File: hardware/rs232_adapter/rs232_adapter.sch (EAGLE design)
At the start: 9 parts, among them IC1 MAX202ECWE

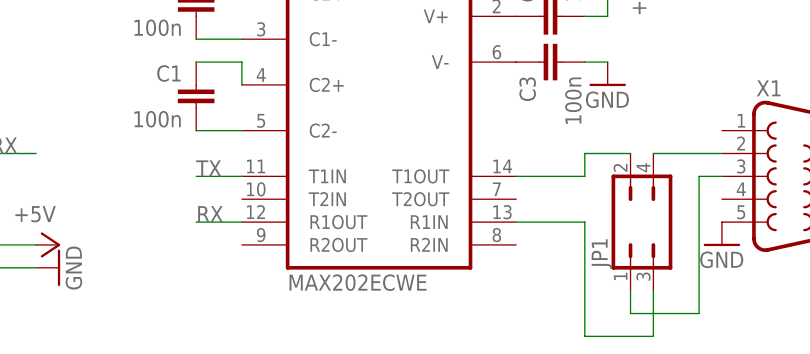
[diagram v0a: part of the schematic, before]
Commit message: change the package of the max202 and add some documentation
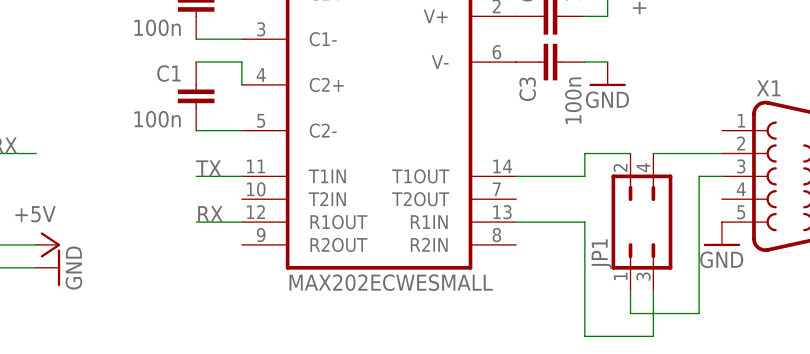
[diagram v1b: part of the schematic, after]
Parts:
- IC1: value MAX202ECWE -> MAX202ECWESMALL; device maxim:MAX202ECWE -> maxim:MAX202ECWESMALL
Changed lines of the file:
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@@
 <part name="GND3" library="supply1" deviceset="GND" device=""/>
 <part name="GND4" library="supply1" deviceset="GND" device=""/>
-<part name="IC1" library="maxim" deviceset="MAX202ECWE" device=""/>
 <part name="C1" library="rcl" deviceset="C-EU" device="C0805" value="100n"/>
 <part name="C2" library="rcl" deviceset="C-EU" device="C0805" value="100n"/>
@@
 <part name="X1" library="con-subd" deviceset="F09" device="HP"/>
 <part name="GND6" library="supply1" deviceset="GND" device=""/>
+<part name="IC1" library="maxim" deviceset="MAX202ECWE" device="SMALL"/>
 </parts>
 <sheets>
@@
 <instance part="GND3" gate="1" x="0" y="7.62" rot="R270"/>
 <instance part="GND4" gate="1" x="30.48" y="7.62" rot="R90"/>
-<instance part="IC1" gate="G$1" x="66.04" y="25.4"/>
 <instance part="C1" gate="G$1" x="45.72" y="27.94" rot="MR0"/>
 <instance part="C2" gate="G$1" x="45.72" y="38.1" rot="MR0"/>
-<instance part="IC1" gate="P" x="63.5" y="55.88"/>
 <instance part="C3" gate="G$1" x="83.82" y="30.48" rot="MR270"/>
 <instance part="GND1" gate="1" x="91.44" y="27.94"/>
@@
 <instance part="X1" gate="G$1" x="111.76" y="17.78"/>
 <instance part="GND6" gate="1" x="104.14" y="10.16"/>
+<instance part="IC1" gate="G$1" x="66.04" y="25.4"/>
+<instance part="IC1" gate="P" x="63.5" y="55.88"/>
 </instances>
 <busses>
@@
 </segment>
 <segment>
-<pinref part="IC1" gate="G$1" pin="R1OUT"/>
 <wire x1="50.8" y1="12.7" x2="45.72" y2="12.7" width="0.1524" layer="91"/>
 <label x="45.72" y="12.7" size="1.778" layer="95"/>
+<pinref part="IC1" gate="G$1" pin="R1OUT"/>
 </segment>
 </net>
@@
 </segment>
 <segment>
-<pinref part="IC1" gate="G$1" pin="T1IN"/>
 <wire x1="50.8" y1="17.78" x2="45.72" y2="17.78" width="0.1524" layer="91"/>
 <label x="45.72" y="17.78" size="1.778" layer="95"/>
+<pinref part="IC1" gate="G$1" pin="T1IN"/>
 </segment>
 </net>
@@
 <pinref part="SV2" gate="G$1" pin="17"/>
 <wire x1="2.54" y1="10.16" x2="7.62" y2="10.16" width="0.1524" layer="91"/>
-</segment>
-<segment>
-<pinref part="IC1" gate="P" pin="VCC"/>
-<pinref part="P+1" gate="1" pin="+5V"/>
 </segment>
 <segment>
@@
 <pinref part="P+3" gate="1" pin="+5V"/>
 </segment>
+<segment>
+<pinref part="P+1" gate="1" pin="+5V"/>
+<pinref part="IC1" gate="P" pin="VCC"/>
+</segment>
 </net>
 <net name="GND" class="0">
@@
 </segment>
 <segment>
-<pinref part="IC1" gate="P" pin="GND"/>
-<pinref part="GND2" gate="1" pin="GND"/>
-</segment>
-<segment>
 <pinref part="C5" gate="G$1" pin="2"/>
 <pinref part="GND5" gate="1" pin="GND"/>
@@
 <pinref part="GND6" gate="1" pin="GND"/>
 </segment>
+<segment>
+<pinref part="GND2" gate="1" pin="GND"/>
+<pinref part="IC1" gate="P" pin="GND"/>
+</segment>
 </net>
 <net name="N$1" class="0">
 <segment>
 <pinref part="C1" gate="G$1" pin="2"/>
+<wire x1="45.72" y1="22.86" x2="50.8" y2="22.86" width="0.1524" layer="91"/>
 <pinref part="IC1" gate="G$1" pin="C2-"/>
-<wire x1="45.72" y1="22.86" x2="50.8" y2="22.86" width="0.1524" layer="91"/>
 </segment>
 </net>
@@
 <segment>
 <pinref part="C2" gate="G$1" pin="2"/>
+<wire x1="45.72" y1="33.02" x2="50.8" y2="33.02" width="0.1524" layer="91"/>
 <pinref part="IC1" gate="G$1" pin="C1-"/>
-<wire x1="45.72" y1="33.02" x2="50.8" y2="33.02" width="0.1524" layer="91"/>
 </segment>
 </net>
@@
 </segment>
 </net>
-<net name="N$5" class="0">
-<segment>
-<pinref part="IC1" gate="G$1" pin="V-"/>
-<pinref part="C3" gate="G$1" pin="1"/>
-</segment>
-</net>
-<net name="N$6" class="0">
-<segment>
-<pinref part="IC1" gate="G$1" pin="V+"/>
-<pinref part="C4" gate="G$1" pin="1"/>
-</segment>
-</net>
 <net name="N$7" class="0">
 <segment>
-<pinref part="IC1" gate="G$1" pin="T1OUT"/>
 <wire x1="81.28" y1="17.78" x2="88.9" y2="17.78" width="0.1524" layer="91"/>
 <wire x1="88.9" y1="17.78" x2="88.9" y2="20.32" width="0.1524" layer="91"/>
 <pinref part="JP1" gate="B1" pin="2"/>
 <wire x1="88.9" y1="20.32" x2="93.98" y2="20.32" width="0.1524" layer="91"/>
+<pinref part="IC1" gate="G$1" pin="T1OUT"/>
 </segment>
 </net>
@@
 <wire x1="88.9" y1="0" x2="96.52" y2="0" width="0.1524" layer="91"/>
 <wire x1="96.52" y1="0" x2="96.52" y2="5.08" width="0.1524" layer="91"/>
+<wire x1="81.28" y1="12.7" x2="88.9" y2="12.7" width="0.1524" layer="91"/>
 <pinref part="IC1" gate="G$1" pin="R1IN"/>
-<wire x1="81.28" y1="12.7" x2="88.9" y2="12.7" width="0.1524" layer="91"/>
 </segment>
 </net>
@@
 </segment>
 </net>
+<net name="N$5" class="0">
+<segment>
+<pinref part="C3" gate="G$1" pin="1"/>
+<pinref part="IC1" gate="G$1" pin="V-"/>
+</segment>
+</net>
+<net name="N$6" class="0">
+<segment>
+<pinref part="C4" gate="G$1" pin="1"/>
+<pinref part="IC1" gate="G$1" pin="V+"/>
+</segment>
+</net>
